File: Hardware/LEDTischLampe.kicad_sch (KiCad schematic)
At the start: 31 parts, among them IC1 RY8310, J1 Conn_01x02_Socket, J2 USB_C_Receptacle_USB2.0_14P, J3 Conn_02x03_Counter_Clockwise, M1 P-CHANNEL-MOSFET, SW1 Reset, SW2 User, U1 ESP32-C3-WROOM-02

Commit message: edit layout
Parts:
- added H1, H2: MountingHole, MountingHole:MountingHole_3.2mm_M3, symbol Mechanical:MountingHole
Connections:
- net UserButton is gone; now on net IO9: C8.1, R13.2, SW2.2
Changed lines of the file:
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@@
 		)
 	)
+	(global_label "IO9"
+		(shape input)
+		(at 99.06 193.04 0)
+		(fields_autoplaced yes)
+		(effects
+			(font
+				(size 1.27 1.27)
+			)
+			(justify left)
+		)
+		(property "Intersheetrefs" "${INTERSHEET_REFS}"
+			(at 105.19 193.04 0)
+			(effects
+				(font
+					(size 1.27 1.27)
+				)
+				(justify left)
+				(hide yes)
+			)
+		)
+	)
 	(global_label "StateLed01"
 		(shape input)
@@
 		)
 	)
-	(global_label "UserButton"
-		(shape input)
-		(at 99.06 193.04 0)
-		(fields_autoplaced yes)
-		(effects
-			(font
-				(size 1.27 1.27)
-			)
-			(justify left)
-		)
-		(property "Intersheetrefs" "${INTERSHEET_REFS}"
-			(at 111.875 192.9606 0)
-			(effects
-				(font
-					(size 1.27 1.27)
-				)
-				(justify left)
-				(hide yes)
-			)
-		)
-	)
 	(global_label "DN"
 		(shape input)
@@
 	)
 	(symbol
+		(lib_id "Mechanical:MountingHole")
+		(at 276.86 267.97 0)
+		(unit 1)
+		(exclude_from_sim yes)
+		(in_bom no)
+		(on_board yes)
+		(dnp no)
+		(fields_autoplaced yes)
+		(property "Reference" "H1"
+			(at 279.4 266.6999 0)
+			(effects
+				(font
+					(size 1.27 1.27)
+				)
+				(justify left)
+			)
+		)
+		(property "Value" "MountingHole"
+			(at 279.4 269.2399 0)
+			(effects
+				(font
+					(size 1.27 1.27)
+				)
+				(justify left)
+			)
+		)
+		(property "Footprint" "MountingHole:MountingHole_3.2mm_M3"
+			(at 276.86 267.97 0)
+			(effects
+				(font
+					(size 1.27 1.27)
+				)
+				(hide yes)
+			)
+		)
+		(property "Datasheet" "~"
+			(at 276.86 267.97 0)
+			(effects
+				(font
+					(size 1.27 1.27)
+				)
+				(hide yes)
+			)
+		)
+		(property "Description" "Mounting Hole without connection"
+			(at 276.86 267.97 0)
+			(effects
+				(font
+					(size 1.27 1.27)
+				)
+				(hide yes)
+			)
+		)
+		(instances
+			(project ""
+				(path "/34c772aa-2c68-48ca-93c3-7ad335c6d96d"
+					(reference "H1")
+					(unit 1)
+				)
+			)
+		)
+	)
+	(symbol
 		(lib_id "Device:R")
 		(at 49.53 50.8 0)
@@
 					(unit 1)
 				)
+			)
+		)
+	)
+	(symbol
+		(lib_id "Mechanical:MountingHole")
+		(at 251.46 267.97 0)
+		(unit 1)
+		(exclude_from_sim yes)
+		(in_bom no)
+		(on_board yes)
+		(dnp no)
+		(fields_autoplaced yes)
+		(property "Reference" "H2"
+			(at 254 266.6999 0)
+			(effects
+				(font
+					(size 1.27 1.27)
+				)
+				(justify left)
+			)
+		)
+		(property "Value" "MountingHole"
+			(at 254 269.2399 0)
+			(effects
+				(font
+					(size 1.27 1.27)
+				)
+				(justify left)
+			)
+		)
+		(property "Footprint" "MountingHole:MountingHole_3.2mm_M3"
+			(at 251.46 267.97 0)
+			(effects
+				(font
+					(size 1.27 1.27)
+				)
+				(hide yes)
+			)
+		)
+		(property "Datasheet" "~"
+			(at 251.46 267.97 0)
+			(effects
+				(font
+					(size 1.27 1.27)
+				)
+				(hide yes)
+			)
+		)
+		(property "Description" "Mounting Hole without connection"
+			(at 251.46 267.97 0)
+			(effects
+				(font
+					(size 1.27 1.27)
+				)
+				(hide yes)
+			)
+		)
+		(instances
+			(project "LEDTischLampe"
+				(path "/34c772aa-2c68-48ca-93c3-7ad335c6d96d"
+					(reference "H2")
+					(unit 1)
+				)

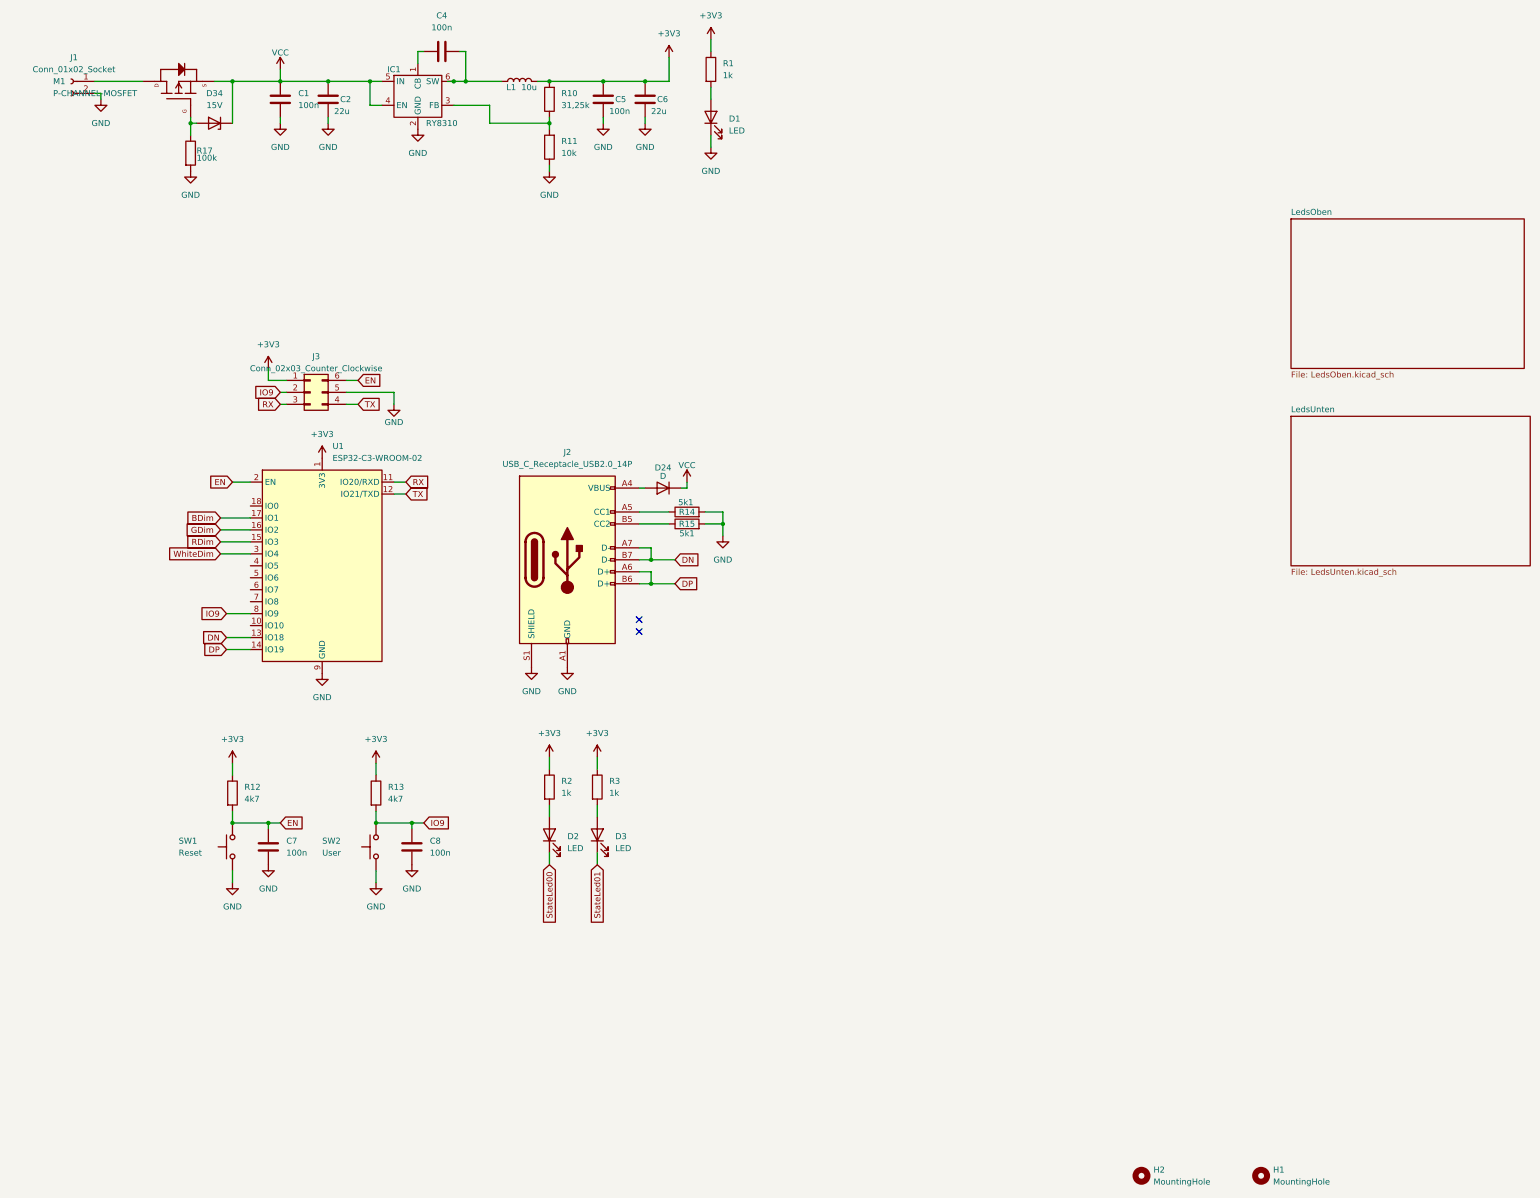
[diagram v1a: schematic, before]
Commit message: finished preliminary routing
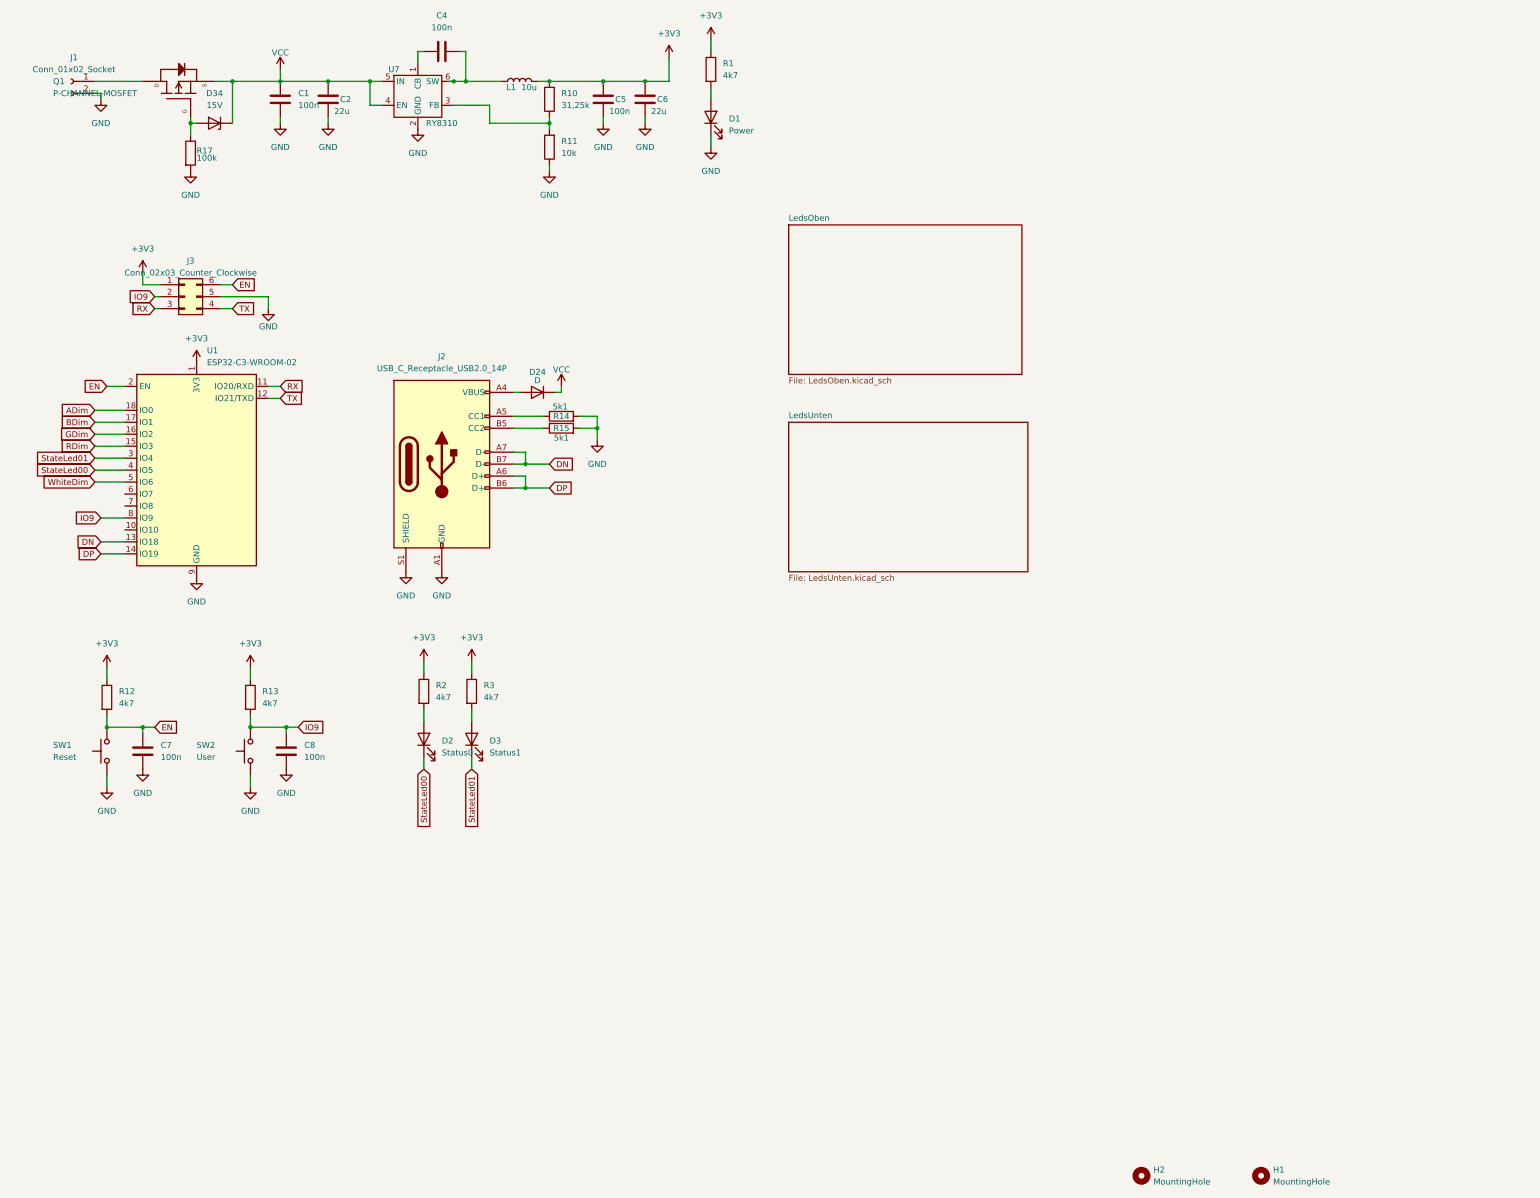
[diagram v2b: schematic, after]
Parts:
- D1: value LED -> Power; footprint LED_SMD:LED_0402_1005Metric -> LED_SMD:LED_0805_2012Metric
- D2: value LED -> Status0; footprint LED_SMD:LED_0402_1005Metric -> LED_SMD:LED_0805_2012Metric
- D3: value LED -> Status1; footprint LED_SMD:LED_0402_1005Metric -> LED_SMD:LED_0805_2012Metric
- R1, R2, R3: value 1k -> 4k7
- renumbered M1 to Q1, IC1 to U7
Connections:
- net StateLed00: now also U1.4 (IO5)
- net StateLed01: now also U1.3 (IO4)
- net WhiteDim: now also U1.5 (IO6); no longer U1.3 (IO4)
- net ADim: now reaches U1.18 (IO0)
- no-connect marks 2 -> 0
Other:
- moved on the sheet: C7, C8, D2, D24, D3, J2, J3, R12, R13, R14, R15, R2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

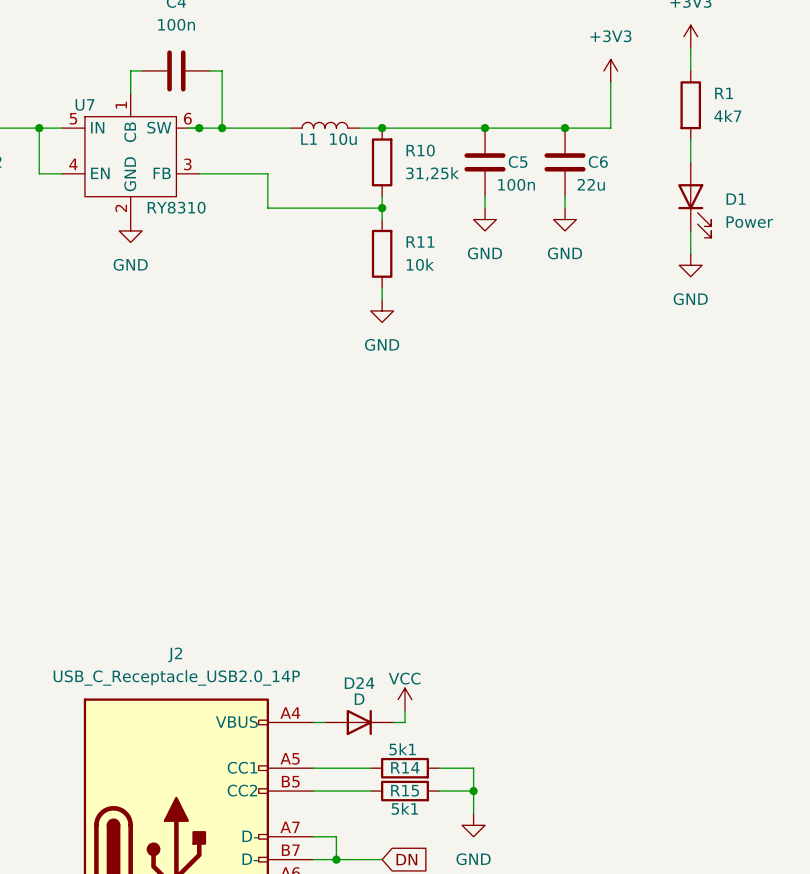
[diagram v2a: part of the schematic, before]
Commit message: assign most LCSC numbers
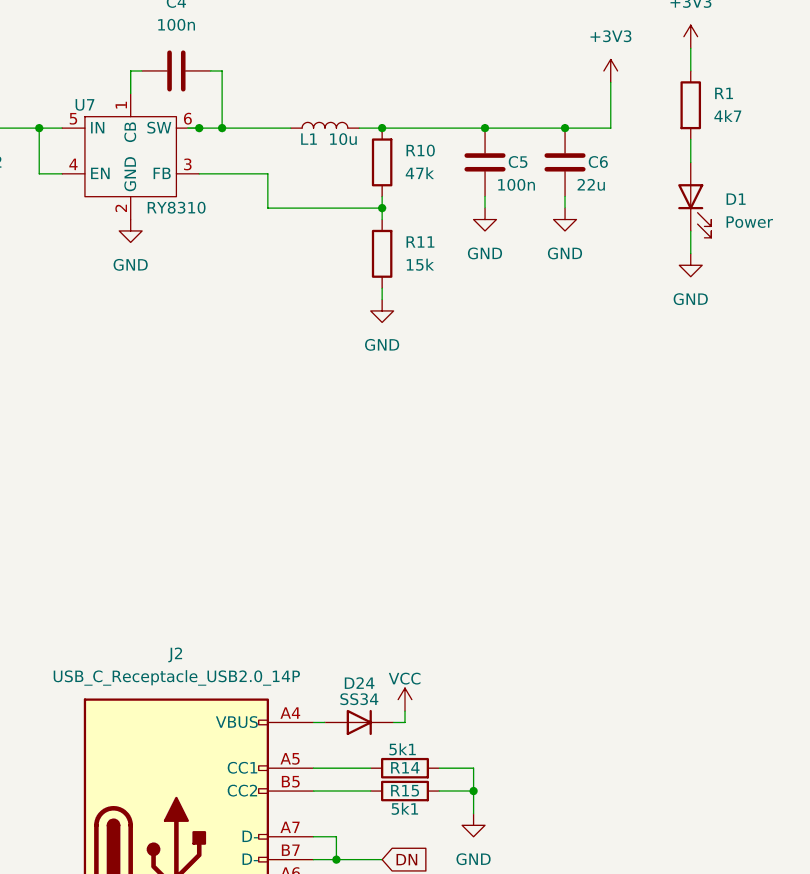
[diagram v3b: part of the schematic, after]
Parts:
- D24: value D -> SS34
- R10: value 31,25k -> 47k
- R11: value 10k -> 15k
- R12, R13: footprint Capacitor_SMD:C_0402_1005Metric -> Resistor_SMD:R_0402_1005Metric
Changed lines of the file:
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@@
 			)
 		)
-		(property "Footprint" "Capacitor_SMD:C_0402_1005Metric"
+		(property "Footprint" "Resistor_SMD:R_0402_1005Metric"
 			(at 29.972 166.37 90)
 			(effects
@@
 			)
 		)
-		(property "Value" "10k"
+		(property "Value" "15k"
 			(at 128.27 50.7999 0)
 			(effects
@@
 			)
 		)
-		(property "Value" "31,25k"
+		(property "Value" "47k"
 			(at 128.27 40.6399 0)
 			(effects
@@
 			)
 		)
-		(property "Value" "D"
+		(property "Value" "SS34"
 			(at 123.19 99.06 0)
 			(effects
@@
 			)
 		)
-		(property "Footprint" "Capacitor_SMD:C_0402_1005Metric"
+		(property "Footprint" "Resistor_SMD:R_0402_1005Metric"
 			(at 60.452 166.37 90)
 			(effects

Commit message: remove LCSC numbers from silkscreen (bug in jlcpcb-tools)
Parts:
- C1, C4, C5, C7, C8: LCSC (none) -> C307331
- C2, C6: LCSC (none) -> C52306
- D1: LCSC (none) -> C84256
- D2: LCSC (none) -> C2296
- D24: LCSC (none) -> C8678
- D3: LCSC (none) -> C2297
- J2: LCSC (none) -> C2927038
- L1: LCSC (none) -> C5832376
- Q1: LCSC (none) -> C471913
- R1, R12, R13, R2, R3: LCSC (none) -> C25900
- R10: LCSC (none) -> C25792
- R11: LCSC (none) -> C25756
- R14, R15: LCSC (none) -> C25905
- R17: LCSC (none) -> C25741
- SW1, SW2: LCSC (none) -> C318884
- U1: LCSC (none) -> C2934560
- U7: LCSC (none) -> C370876
